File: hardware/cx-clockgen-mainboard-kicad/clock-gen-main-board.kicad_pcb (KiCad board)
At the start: 2 copper layers, 70 x 64.4 mm, 21 parts, among them J1 Conn_01x03_Pin, J2 Conn_01x03_Pin, J3 Headswitch_SMA, J4 Conn_01x01_Pin, J5 Conn_01x01_Pin, J6 Conn_01x01_Pin, J7 Conn_01x01_Pin, J8 Conn_Coaxial, U1 Pico

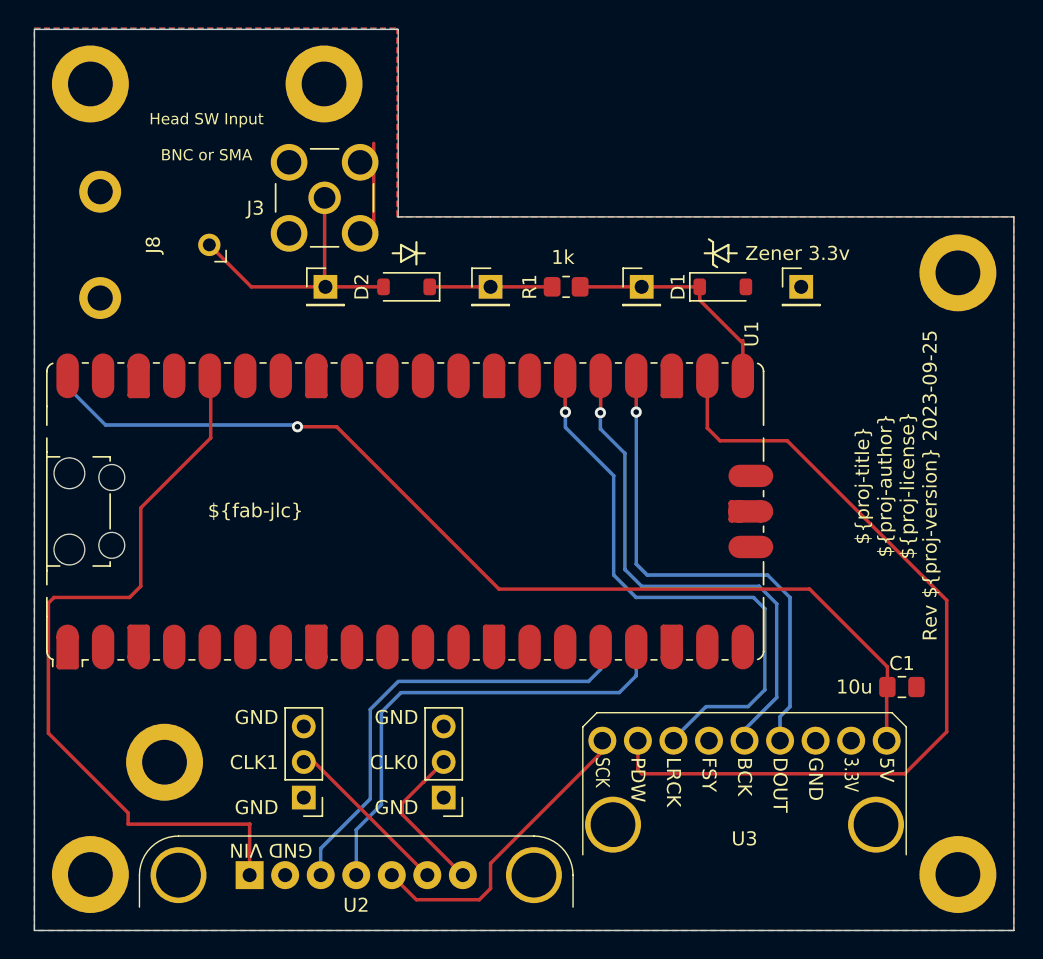
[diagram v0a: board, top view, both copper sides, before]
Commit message: Added missing setup shell scripts
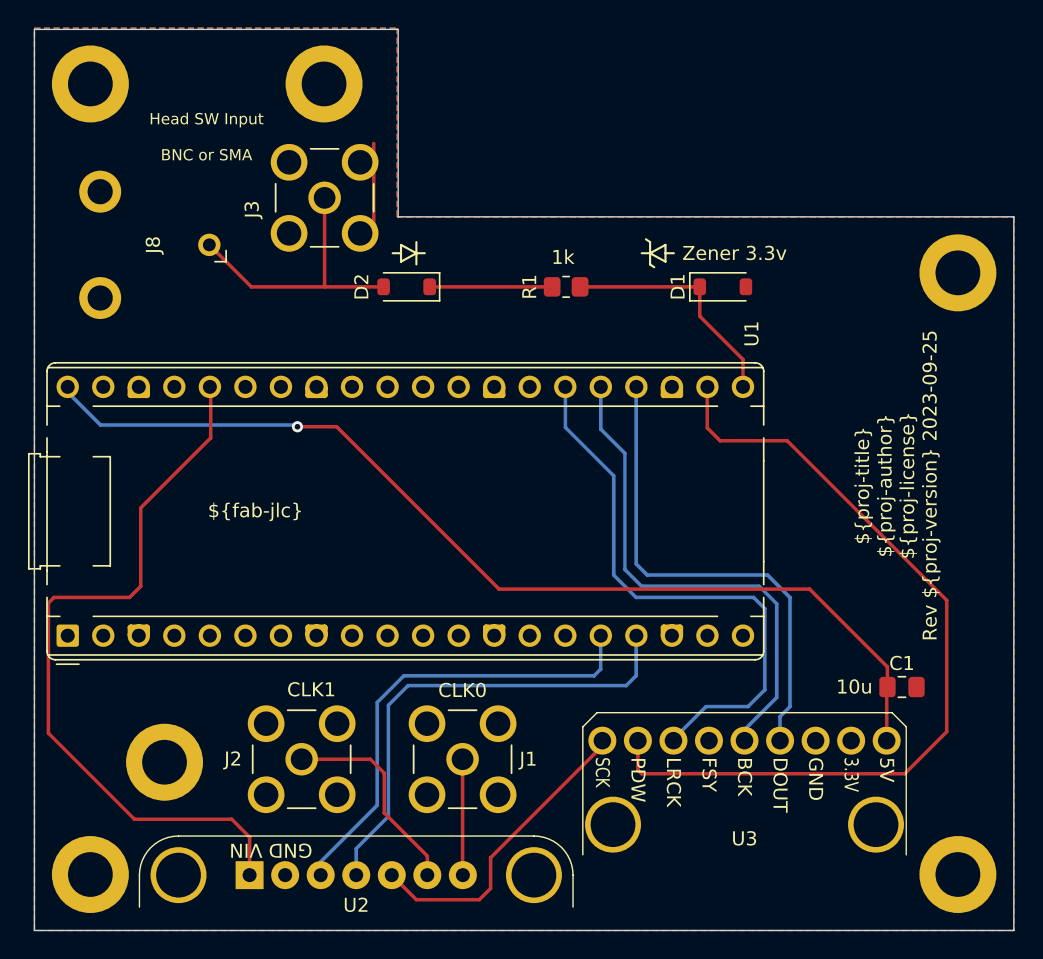
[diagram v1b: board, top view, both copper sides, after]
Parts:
- removed J4, J5, J6, J7: Conn_01x01_Pin, Connector_PinHeader_2.54mm:PinHeader_1x01_P2.54mm_Vertical
- J1, J2: footprint Connector_PinHeader_2.54mm:PinHeader_1x03_P2.54mm_Vertical -> Clockgen Footprints:GRADCONN_RFPC-SMA28-F
- J3: footprint RFPC_SMA28_F:GRADCONN_RFPC-SMA28-F -> Clockgen Footprints:GRADCONN_RFPC-SMA28-F
- U1: footprint Module:RaspberryPi_Pico_SMD_HandSolder -> Module:RaspberryPi_Pico_Common_THT
- moved U1 25.7 mm to (100.4, 108.9)
- moved J1 3.05 mm to (128.6, 117.8), turned to 0 degrees
- moved J2 2.74 mm to (117.1, 117.8), turned to 0 degrees
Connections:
- J1 pad 1: GND -> Net-(U2-CLK0)
- J2 pad 1: GND -> Net-(U2-CLK1)
- U2 pad 0: Net-(J1-Pin_2) -> Net-(U2-CLK0)
- U2 pad 1: Net-(J2-Pin_2) -> Net-(U2-CLK1)
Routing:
- net Net-(U2-CLK1): track 0.00 -> 14.9 mm
- net Net-(J2-Pin_2): track 12.2 -> 0.00 mm
- net Net-(J1-Pin_2): track 11.1 -> 0.00 mm
- net Net-(U2-CLK0): track 0.00 -> 8.29 mm
- net /Gen.VSI: track 54.1 -> 53.0 mm
- net /PCM.LRClk: track 41.5 -> 40.6 mm, vias 1 -> 0
- net /PCM.BitClk: track 37.2 -> 36.4 mm, vias 1 -> 0
- net /PCM.Data: track 36.0 -> 35.2 mm, vias 1 -> 0
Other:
- outline, holes or cut-outs redrawn
- board text added: "CLK0"
- board text added: "CLK1"
- board text removed: "GND CLK0 GND"
- board text removed: "GND CLK1 GND"

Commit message: Remove obsolete KiCad library files, including symbol, footprint, and 3D model files for ADA4857-1YRZ-R7 and related components, to streamline project resources and eliminate unused assets.
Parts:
- J1, J2, J3: footprint Clockgen Footprints:GRADCONN_RFPC-SMA28-F -> GDH Connectors:GRADCONN_RFPC-SMA28-F
- J8: footprint vhs_decode_footprints:Molex_0731000154_BNC_RA_THT -> GDH Connectors:Molex_0731000154_BNC_RA_THT
- U2: footprint adafruit-si5351:Adafruit_Si5351A_Breakout_Board -> GDH Modules:Adafruit_Si5351A_Breakout_Board
- U3: footprint black-pcm1802:black-pcm1802-board -> GDH Modules:black-pcm1802-board
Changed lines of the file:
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@@
 	(property "proj-title" "clock-gen adc main board")
 	(property "proj-version" "1.0")
-	(footprint "black-pcm1802:black-pcm1802-board"
+	(footprint "GDH Modules:black-pcm1802-board"
 		(layer "F.Cu")
 		(at 148.75 114.4345 180)
@@
 		(embedded_fonts no)
 	)
-	(footprint "vhs_decode_footprints:Molex_0731000154_BNC_RA_THT"
+	(footprint "GDH Connectors:Molex_0731000154_BNC_RA_THT"
 		(layer "F.Cu")
 		(at 110.5 81 90)
@@
 		)
 	)
-	(footprint "Clockgen Footprints:GRADCONN_RFPC-SMA28-F"
+	(footprint "GDH Connectors:GRADCONN_RFPC-SMA28-F"
 		(layer "F.Cu")
 		(at 118.74 77.64 90)
@@
 		)
 	)
-	(footprint "Clockgen Footprints:GRADCONN_RFPC-SMA28-F"
+	(footprint "GDH Connectors:GRADCONN_RFPC-SMA28-F"
 		(layer "F.Cu")
 		(at 128.6 117.76)
@@
 		)
 	)
-	(footprint "Clockgen Footprints:GRADCONN_RFPC-SMA28-F"
+	(footprint "GDH Connectors:GRADCONN_RFPC-SMA28-F"
 		(layer "F.Cu")
 		(at 117.1 117.76)
@@
 		(embedded_fonts no)
 	)
-	(footprint "adafruit-si5351:Adafruit_Si5351A_Breakout_Board"
+	(footprint "GDH Modules:Adafruit_Si5351A_Breakout_Board"
 		(layer "F.Cu")
 		(at 121 123.25 180)
